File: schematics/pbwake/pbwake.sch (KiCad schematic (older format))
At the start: 11 parts, among them J1 USB_A, J2 USB_A, J3 DEBUG, J4 AVR-ISP-6, Q1 IRF530, U1 ATtinyXX-20PU

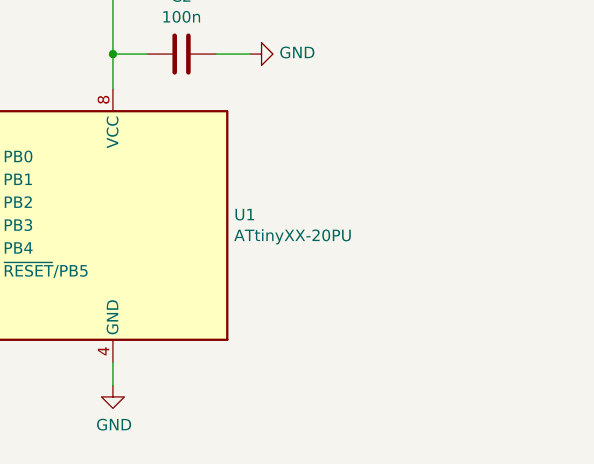
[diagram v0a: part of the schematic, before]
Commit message: schematics: Add uc types
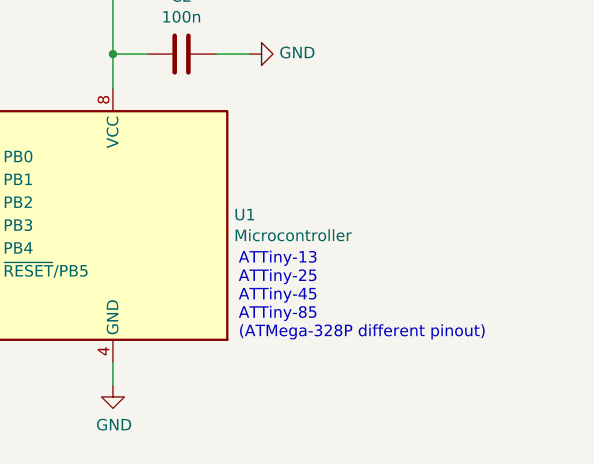
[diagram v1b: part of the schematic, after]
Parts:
- U1: value ATtinyXX-20PU -> Microcontroller
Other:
- note added: "ATTiny-13\nATTiny-25\nATTiny-45\nATTiny-85\n(ATMega-328P different pinout)"
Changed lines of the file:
@@
 Sheet 1 1
 Title "pbwake"
-Date "2020-07-04"
+Date "2020-07-17"
 Rev "1.0"
 Comp "Michael Buesch <m@bues.ch>"
@@
 P 8600 4950
 F 0 "U1" H 8070 4996 50  0000 R CNN
-F 1 "ATtinyXX-20PU" H 8070 4905 50  0000 R CNN
+F 1 "Microcontroller" H 8070 4905 50  0000 R CNN
 F 2 "Package_DIP:DIP-8_W7.62mm" H 8600 4950 50  0001 C CIN
 F 3 "http://ww1.microchip.com/downloads/en/DeviceDoc/doc2535.pdf" H 8600 4950 50  0001 C CNN
@@
 Connection ~ 6850 4650
 NoConn ~ 8000 4950
+Text Notes 9150 5450 0    50   ~ 0
+ATTiny-13\nATTiny-25\nATTiny-45\nATTiny-85\n(ATMega-328P different pinout)
 $EndSCHEMATC
